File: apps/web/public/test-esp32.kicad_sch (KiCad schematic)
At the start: 9 parts, among them J1 USB_5V, SW1 EN_BTN, U1 ESP32-WROOM-32, U2 AMS1117-3.3

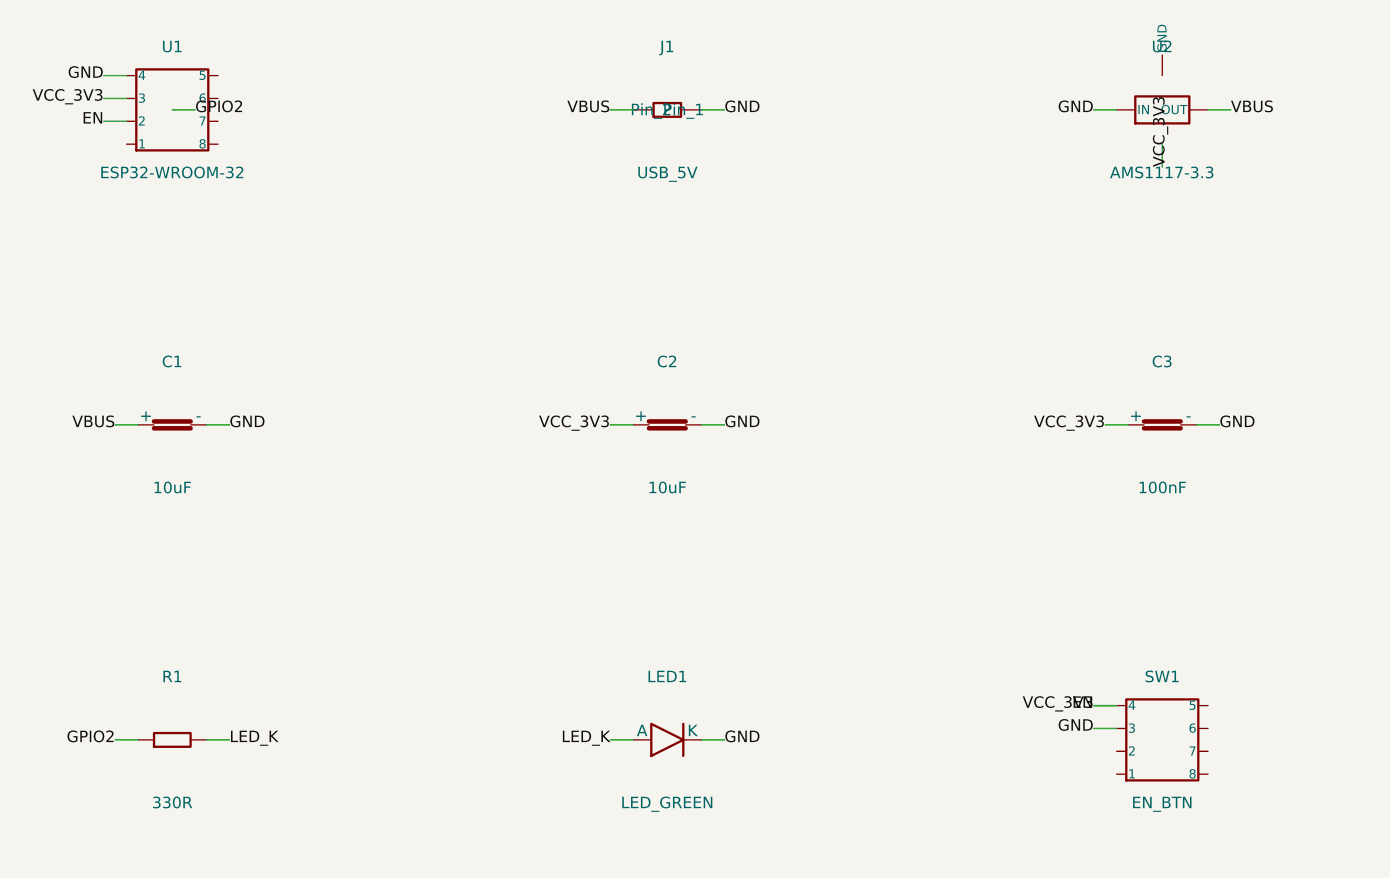
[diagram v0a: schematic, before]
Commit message: fix(schematic): bump margin_side to 38mm + comp_w_span to 20mm for long net-labels
Previous 28mm margin was OK for short labels (VIN, GND) but insufficient
for longer labels like VCC_3V3, LED_GREEN, GND_R2 (~18mm from body centre).
On the ESP32 test schematic, labels GND/VCC_3V3/EN of U1 still touched
the inner frame border.

New values:
- margin_side  = 38mm (was 28) — body origin 38, label text reaches x=20,
  inner frame at x=10 -> 10mm clearance for longest labels
- comp_w_span  = 20mm (was 15) — symmetric clearance on the right side

Paper width grows 181 -> 206mm. All 3 test schematics regenerated.
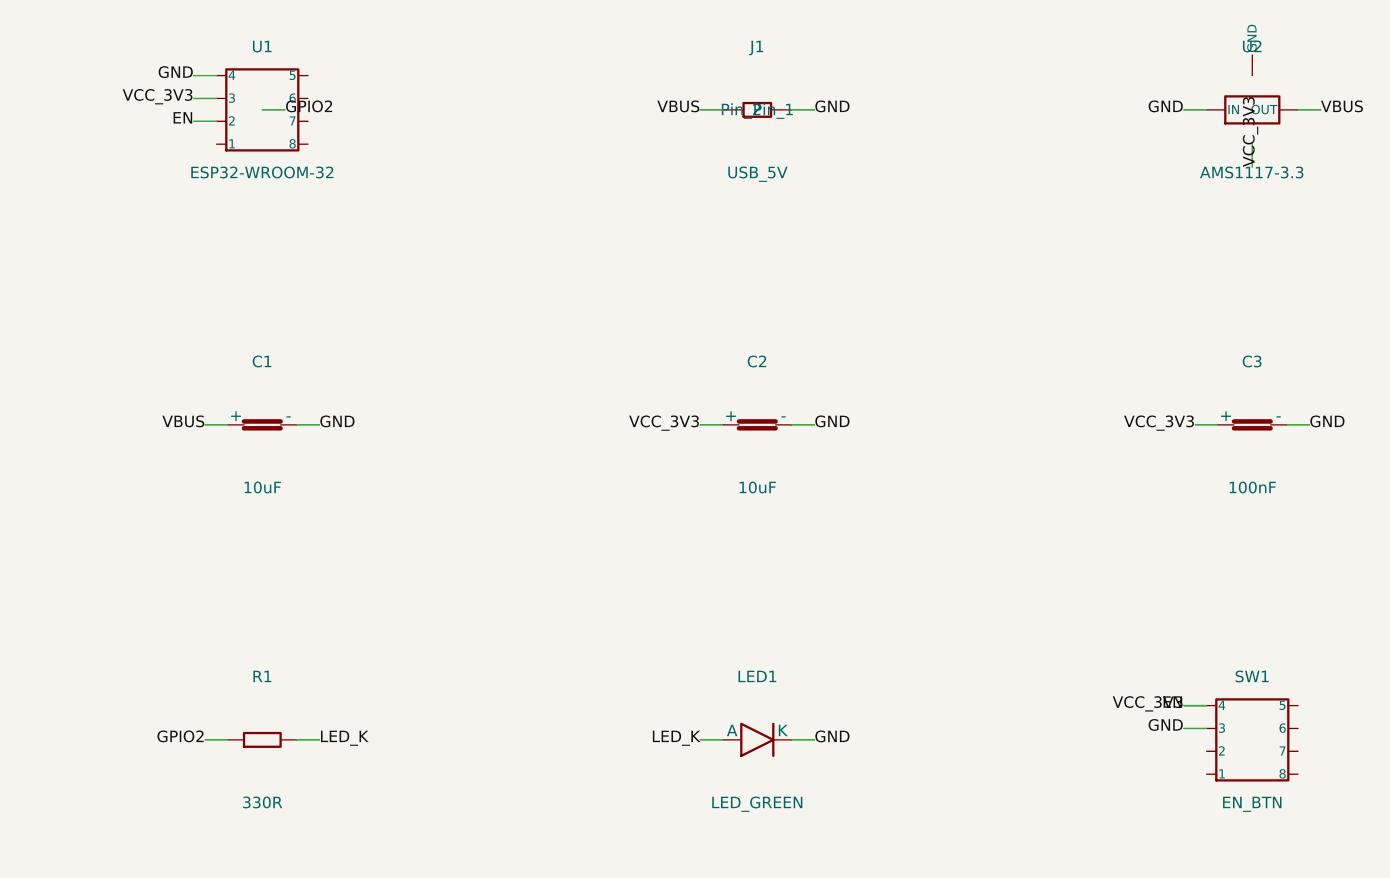
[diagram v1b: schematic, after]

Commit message: fix(schematic): more breathing room — bump margin_top to 25mm + TITLE_PADDING to 15mm
Component names (Reference U1/C1/J1 + Value LM7805/330nF/VIN_CONN) were
visually too close to the inner frame top border and to the title block
edge. Increased internal margins so all labels sit comfortably inside
the visible inner frame area.

Changes:
- margin_top      20 -> 25 mm  (more space below the upper frame border)
- TITLE_PADDING    6 -> 15 mm  (more space before the title block)
- Paper height grows 123 -> 137 mm (LM7805) / 158 -> 172 mm (NE555/ESP32)
- Regenerated all 3 test schematics

Verified visually: U1+LM7805, C1+330nF, C2+100nF, J1+VIN_CONN,
J2+VOUT_5V all sit inside the inner frame with clear buffer on all sides.
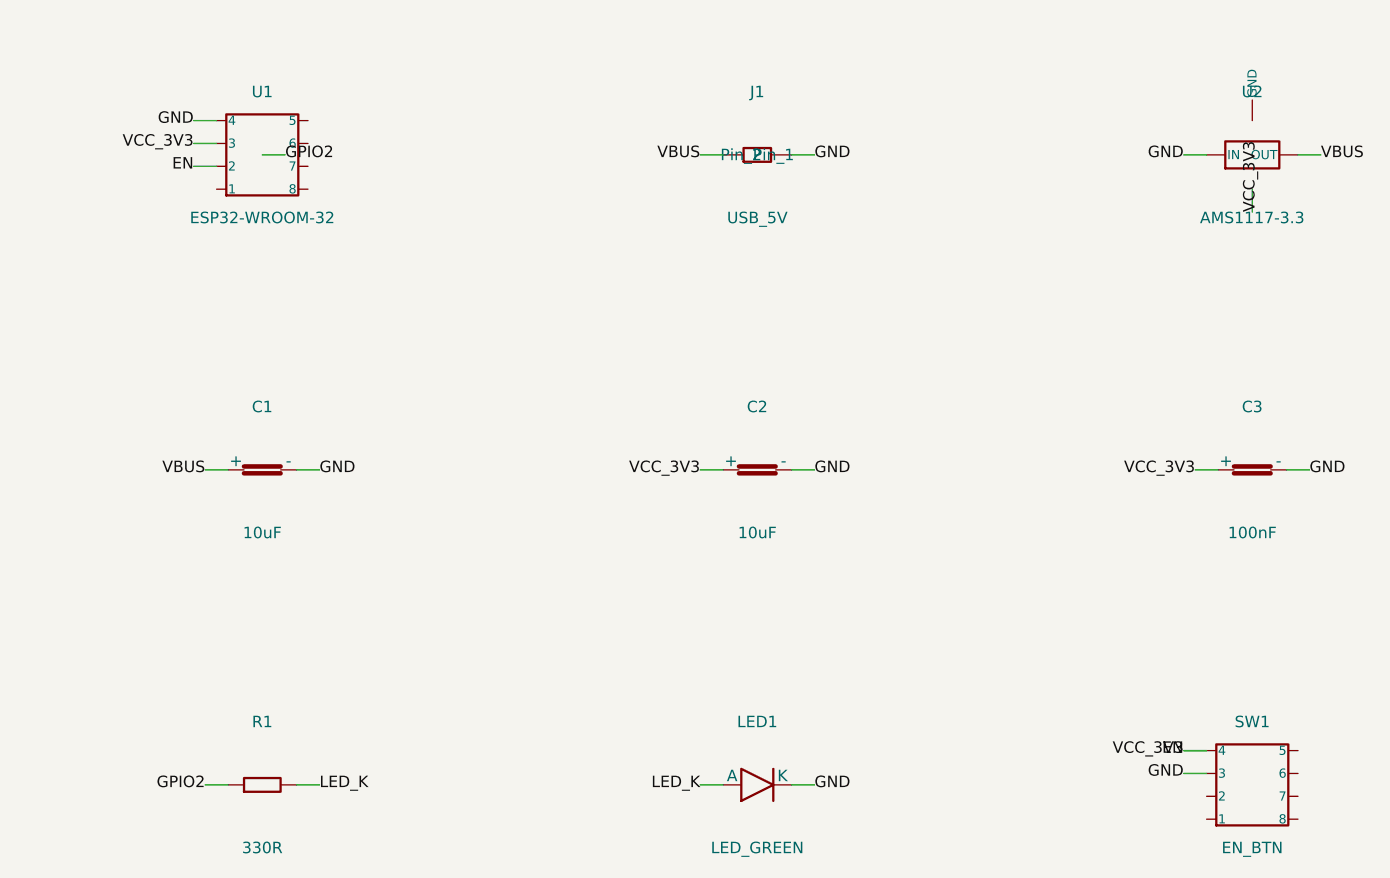
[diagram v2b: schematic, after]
